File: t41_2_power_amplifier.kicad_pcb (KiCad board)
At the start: 2 copper layers, 100 x 100 mm, 72 parts, among them J1 5-1814832-1, J2 5-1814832-1, J3 B2B-XH-A_LF__SN_, J5 Screw_Terminal_01x02, Q1 Q_NMOS_GSD, Q2 Q_NPN_BCE, Q3 Q_NMOS_GSD, Q4 Q_NPN_BCE, Q5 Q_PMOS_GSD, Q6 Q_NPN_BEC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

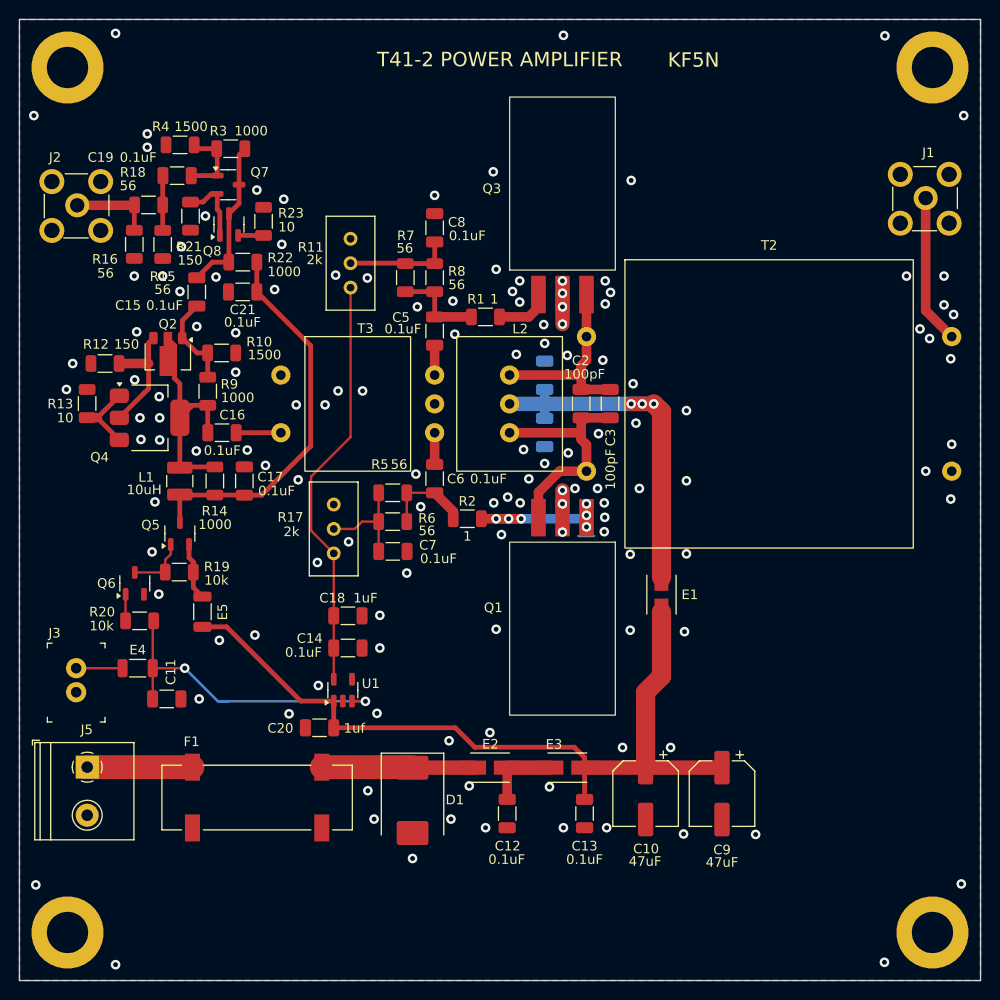
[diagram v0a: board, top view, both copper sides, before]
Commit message: Power Amplifier module ready for fab.
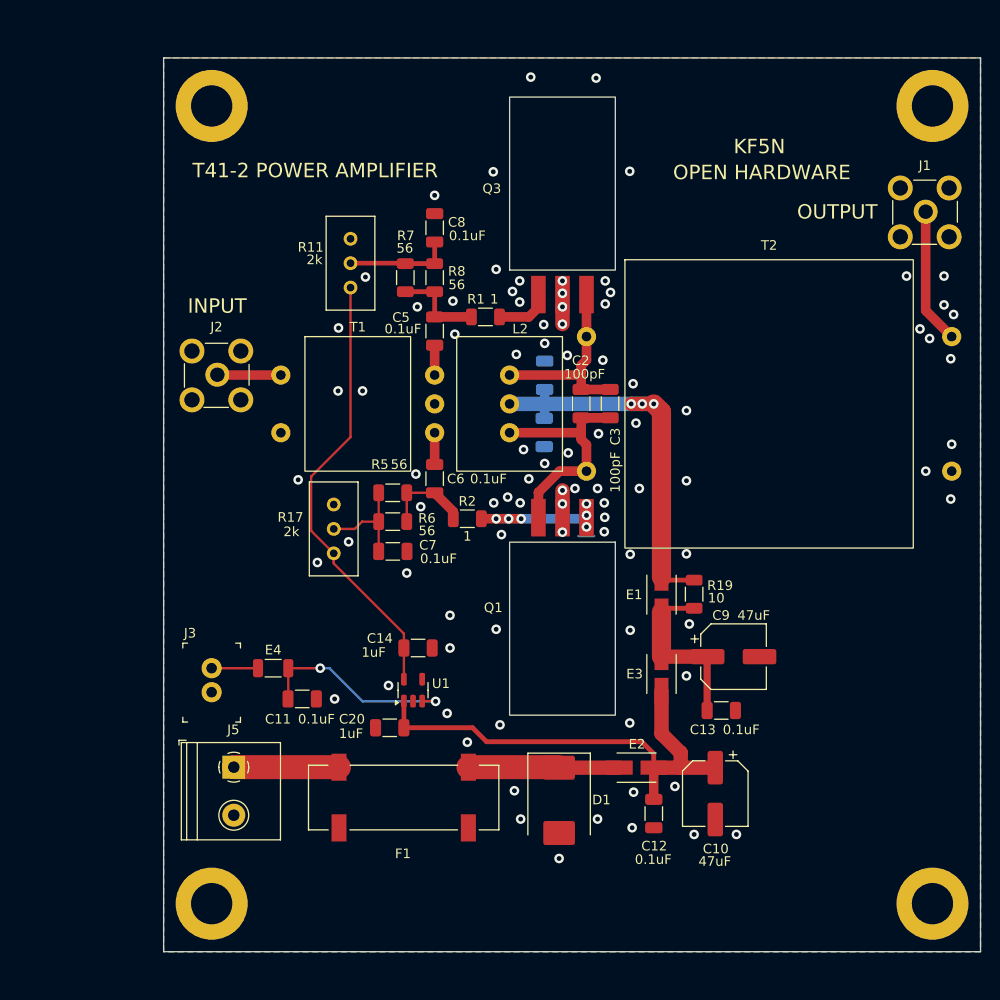
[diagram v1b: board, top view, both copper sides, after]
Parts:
- removed C15, C16, C17, C19, C21: 0.1uF, Capacitor_SMD:C_1206_3216Metric
- removed C18: 1uF, Capacitor_SMD:C_1206_3216Metric
- removed E5: XXX, Inductor_SMD:L_1206_3216Metric
- removed L1: 10uH, Inductor_SMD:L_1210_3225Metric
- removed Q2: Q_NPN_BCE, Package_TO_SOT_SMD:SOT-89-3
- removed Q4: Q_NPN_BCE, Package_TO_SOT_SMD:SOT-223
- removed Q5: Q_PMOS_GSD, Package_TO_SOT_SMD:SOT-23-3
- removed Q6, Q7, Q8: Q_NPN_BEC, Package_TO_SOT_SMD:SOT-23-3
- removed R10, R4: 1500, Resistor_SMD:R_1206_3216Metric
- removed R12, R21: 150, Resistor_SMD:R_1206_3216Metric
- removed R13, R23: 10, Resistor_SMD:R_1206_3216Metric
- removed R14, R22, R3, R9: 1000, Resistor_SMD:R_1206_3216Metric
- removed R15, R16, R18: 56, Resistor_SMD:R_1206_3216Metric
- removed R20: 10k, Resistor_SMD:R_1206_3216Metric
- removed T3: Transformer_1P_SS, Binocular_Core:BN-43-302
- added T1: Transformer_1P_SS, Binocular_Core:BN-43-302, F.Cu at (135.2, 90.0)
- C14: value 0.1uF -> 1uF
- C20: value 1uf -> 1uF
- R19: value 10k -> 10
- moved R19 53.6 mm to (170.2, 109.8), turned to 90 degrees
- moved J2 22.9 mm to (120.5, 87.0)
- moved C13 17.8 mm to (173.0, 121.9), turned to 0 degrees
- moved H1 15.5 mm to (120.0, 59.0)
- moved H2 15.3 mm to (120.0, 142.0)
- moved C12 15.2 mm to (166.0, 132.6)
- moved D1 15.2 mm to (156.2, 131.2)
- moved E2 15.2 mm to (164.2, 127.8)
- moved J5 15.2 mm to (122.3, 127.8)
- moved F1 15.2 mm to (140.0, 131.0)
- moved C9 14.3 mm to (174.3, 116.3), turned to 0 degrees
- moved E4 14.1 mm to (126.4, 117.5)
- moved J3 14.1 mm to (120.0, 117.5)
- moved C11 14.1 mm to (129.4, 120.7)
- moved E3 13.8 mm to (166.8, 118.1), turned to 90 degrees
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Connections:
- C1 pad 1: /12V_OUT_FIL -> /12V_PA
- C10 pad 1: Net-(U1-VIN) -> /12V_FIL
- C12 pad 1: Net-(C12-Pad1) -> /12V_FIL
- C13 pad 1: Net-(U1-VIN) -> Net-(C13-Pad1)
- C20 pad 1: Net-(U1-VIN) -> /12V_FIL
- C4 pad 1: /12V_OUT_FIL -> /12V_PA
- C9 pad 1: Net-(U1-VIN) -> Net-(C13-Pad1)
- E1 pad 1: Net-(U1-VIN) -> Net-(C13-Pad1)
- E1 pad 2: /12V_OUT_FIL -> /12V_PA
- E2 pad 2: Net-(C12-Pad1) -> /12V_FIL
- E3 pad 1: Net-(C12-Pad1) -> /12V_FIL
- E3 pad 2: Net-(U1-VIN) -> Net-(C13-Pad1)
- L2 pad 2: /12V_OUT_FIL -> /12V_PA
- R19 pad 1: Net-(Q5-G) -> Net-(C13-Pad1)
- R19 pad 2: Net-(Q5-S) -> /12V_PA
- U1 pad 1: Net-(U1-VIN) -> /12V_FIL
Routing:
- net Net-(U1-VIN): track 82.6 -> 0.00 mm
- net /12V_FIL: track 0.00 -> 49.9 mm
- net /12V_PA: track 0.00 -> 42.3 mm, vias 0 -> 3
- net /12V_IN_FIL: track 40.2 -> 0.00 mm
- net /12V_OUT_FIL: track 38.7 -> 0.00 mm, vias 3 -> 0
- net Net-(Q2-C): track 24.0 -> 0.00 mm
- net Net-(C13-Pad1): track 0.00 -> 18.7 mm
- net Net-(Q7-C): track 16.5 -> 0.00 mm
- net Net-(Q2-E): track 12.8 -> 0.00 mm
- net /TXRX: track 34.0 -> 21.4 mm
- net Net-(Q2-B): track 9.77 -> 0.00 mm
- net Net-(Q7-B): track 8.07 -> 0.00 mm
- net Net-(C12-Pad1): track 7.77 -> 0.00 mm
- net Net-(Q7-E): track 7.57 -> 0.00 mm
- net Net-(Q4-E): track 7.56 -> 0.00 mm
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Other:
- board size 100 x 100 mm -> 85 x 93 mm
- board text added: "INPUT"
- board text added: "OPEN HARDWARE"
- board text added: "OUTPUT"

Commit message: Larger output balun design to fab.
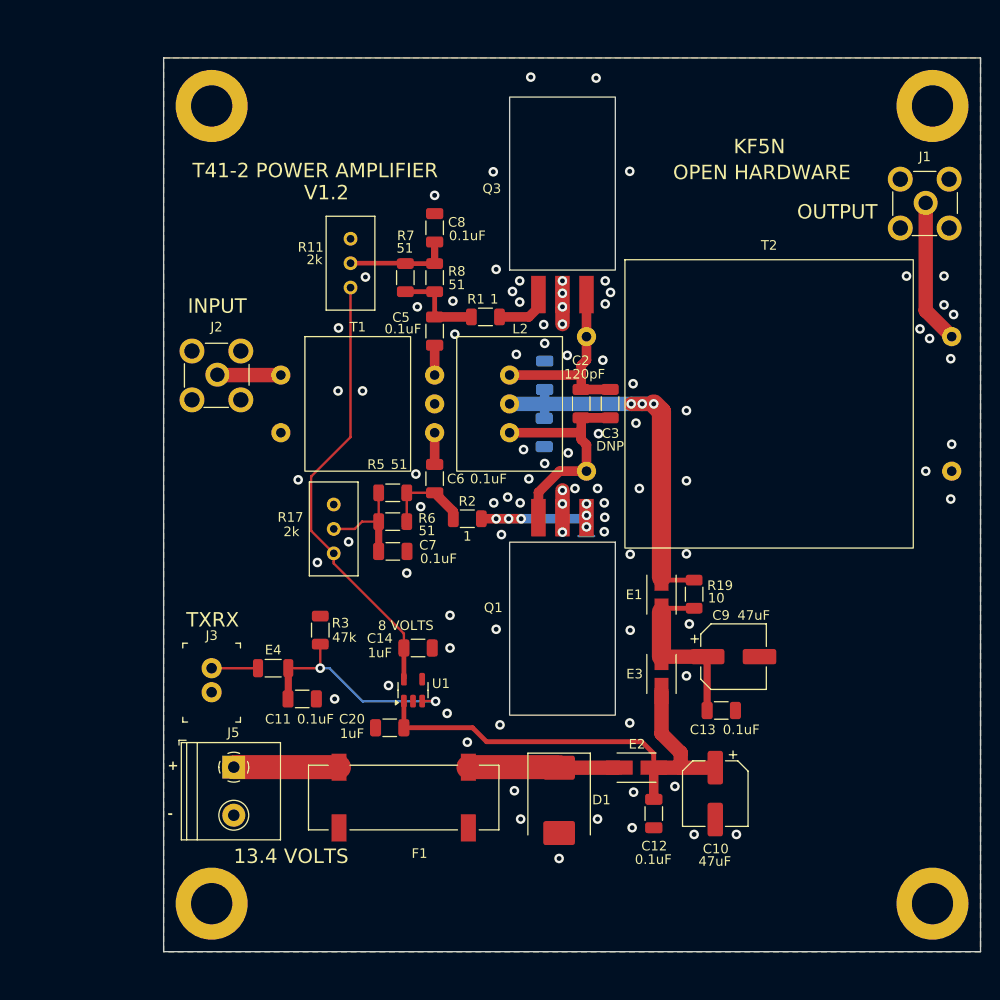
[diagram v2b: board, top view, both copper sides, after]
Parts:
- added R3: 47k, Resistor_SMD:R_1206_3216Metric, F.Cu at (131.3, 113.5)
- C2: value 100pF -> 120pF
- C3: value 100pF -> DNP
- E4: value XXX -> FerriteBead_Small
- R5, R6, R7, R8: value 56 -> 51
- moved J1 0.92 mm to (194.2, 69.2)
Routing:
- net /TXRX: track 21.4 -> 23.9 mm
- net Net-(T2-SB): track 14.1 -> 15.0 mm
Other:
- board text added: "+"
- board text added: "-"
- board text added: "13.4 VOLTS"
- board text added: "8 VOLTS"
- board text added: "TXRX"
- board text added: "V1.2"

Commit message: T41-2 Power Amplifier S to fab.
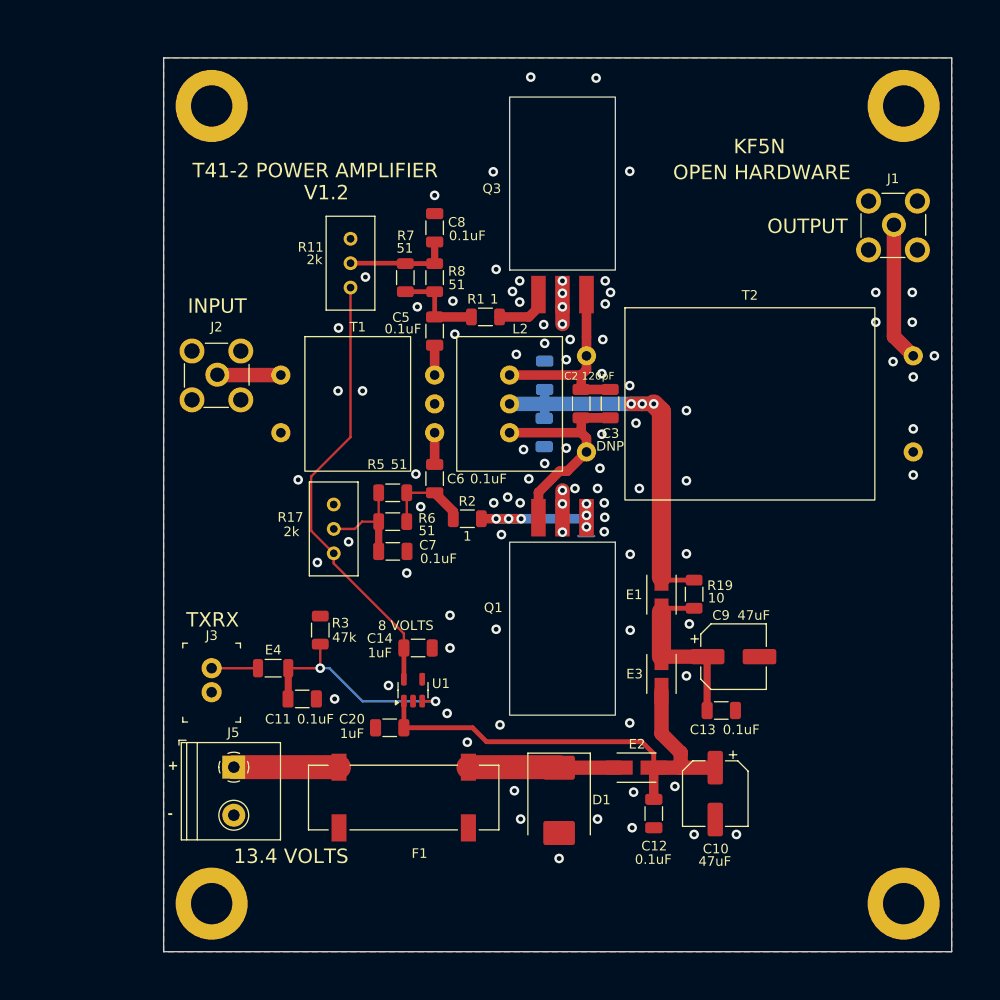
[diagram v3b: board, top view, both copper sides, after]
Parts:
- T2: footprint Binocular_Core:BN-43-7051 -> Binocular_Core:BN-43-3312
- moved J1 4.01 mm to (190.9, 71.4)
- moved H3 3.00 mm to (192.0, 142.0)
- moved H4 3.00 mm to (192.0, 59.0)
- moved T2 2.00 mm to (176.0, 90.0)
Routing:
- net Net-(Q1-D): track 25.4 -> 24.2 mm
- net Net-(T2-SB): track 15.0 -> 14.5 mm
- net GND: vias 89 -> 91
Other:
- board size 85 x 93 mm -> 82 x 93 mm

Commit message: Power Amplifier to fab.
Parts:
- moved J5 1.30 mm to (123.6, 127.8)
- moved J1 0.98 mm to (190.9, 70.5)
- moved J3 0.91 mm to (120.9, 117.5)
- moved C11 0.78 mm to (130.2, 120.7)
- moved E4 0.73 mm to (127.1, 117.5)
- moved F1 0.62 mm to (140.6, 131.0)
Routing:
- net Net-(T2-SB): track 14.5 -> 15.4 mm
- net /TXRX: track 23.9 -> 23.2 mm
- net Net-(J5-Pin_1): track 11.0 -> 10.3 mm
- net Net-(D1-K): track 15.7 -> 15.2 mm
- net GND: vias 91 -> 93
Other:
- board text added: "IN"
- board text added: "V1.3"
- board text removed: "V1.2"
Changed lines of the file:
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@@
 		(pad "4" thru_hole circle
 			(at 8 0)
-			(size 2 2)
-			(drill 1)
+			(size 2.2 2.2)
+			(drill 1.2)
 			(layers "*.Cu" "*.Mask")
 			(remove_unused_layers no)
@@
 	(footprint "3587TR:FUSE_3587TR"
 		(layer "F.Cu")
-		(at 139.98 130.96)
+		(at 140.6 130.96)
 		(property "Reference" "F1"
-			(at 1.645 5.815 0)
+			(at 0 5.84 0)
 			(layer "F.SilkS")
 			(effects
@@
 	(footprint "Capacitor_SMD:C_1206_3216Metric"
 		(layer "F.Cu")
-		(at 129.42 120.7 180)
+		(at 130.2 120.7 180)
 		(descr "Capacitor SMD 1206 (3216 Metric), square (rectangular) end terminal, IPC_7351 nominal, (Body size source: IPC-SM-782 page 76, https://www.pcb-3d.com/wordpress/wp-content/uploads/ipc-sm-782a_amendment_1_and_2.pdf), generated with kicad-footprint-generator")
 		(tags "capacitor")
 		(property "Reference" "C11"
-			(at 2.52 -2.1 180)
+			(at 3.3 -2.1 180)
 			(layer "F.SilkS")
 			(effects
@@
 		)
 		(property "Value" "0.1uF"
-			(at -1.38 -2.1 180)
+			(at -0.6 -2.1 180)
 			(layer "F.SilkS")
 			(effects
@@
 	(footprint "digikey-footprints:RF_SMA_Vertical_5-1814832-1"
 		(layer "F.Cu")
-		(at 190.89 71.44)
+		(at 190.89 70.46)
 		(property "Reference" "J1"
 			(at 0.01 -4.875 0)
@@
 	(footprint "TerminalBlock_Philmore:TerminalBlock_Philmore_TB132_1x02_P5.00mm_Horizontal"
 		(layer "F.Cu")
-		(at 122.3 127.8 -90)
+		(at 123.6 127.8 -90)
 		(descr "Terminal Block Philmore , 2 pins, pitch 5mm, size 10x10.2mm^2, drill diamater 1.2mm, pad diameter 2.4mm, see http://www.philmore-datak.com/mc/Page%20197.pdf, script-generated using https://github.com/pointhi/kicad-footprint-generator/scripts/TerminalBlock_Philmore")
 		(tags "THT Terminal Block Philmore  pitch 5mm size 10x10.2mm^2 drill 1.2mm pad 2.4mm")
 		(property "Reference" "J5"
-			(at -3.6 0.05 180)
+			(at -3.6 0.05 360)
 			(layer "F.SilkS")
 			(effects
@@
 	(footprint "digikey-footprints:PinHeader_1x2_P2.5mm_Drill1.1mm"
 		(layer "F.Cu")
-		(at 119.995 117.5 -90)
+		(at 120.9 117.5 -90)
 		(descr "http://www.jst-mfg.com/product/pdf/eng/eXH.pdf")
 		(property "Reference" "J3"
-			(at -3.4 -0.005 180)
+			(at -3.4 -0.005 360)
 			(layer "F.SilkS")
 			(effects
@@
 	(footprint "Inductor_SMD:L_1206_3216Metric"
 		(layer "F.Cu")
-		(at 126.395 117.5)
+		(at 127.125 117.5)
 		(descr "Inductor SMD 1206 (3216 Metric), square (rectangular) end terminal, IPC_7351 nominal, (Body size source: IPC-SM-782 page 80, https://www.pcb-3d.com/wordpress/wp-content/uploads/ipc-sm-782a_amendment_1_and_2.pdf), generated with kicad-footprint-generator")
 		(tags "inductor")
@@
 		(pad "2" thru_hole circle
 			(at 0 0)
-			(size 2 2)
-			(drill 1)
+			(size 2.2 2.2)
+			(drill 1.2)
 			(layers "*.Cu" "*.Mask")
 			(remove_unused_layers no)
@@
 	)
 	(gr_text "+"
-		(at 115.4 128.2 0)
+		(at 115.2 128.7 0)
 		(layer "F.SilkS")
 		(effects
 			(font
-				(size 1 1)
-				(thickness 0.2)
-				(bold yes)
+				(size 2 2)
+				(thickness 0.3)
 			)
 			(justify left bottom)
@@
 	)
 	(gr_text "-"
-		(at 115.4 133.2 0)
+		(at 115.2 133.7 0)
 		(layer "F.SilkS")
 		(effects
 			(font
-				(size 1 1)
-				(thickness 0.2)
-				(bold yes)
+				(size 2 2)
+				(thickness 0.3)
 			)
 			(justify left bottom)
@@
 		)
 	)
-	(gr_text "V1.2"
+	(gr_text "IN"
+		(at 115.4 118.4 0)
+		(layer "F.SilkS")
+		(effects
+			(font
+				(size 1.5 1.5)
+				(thickness 0.2)
+			)
+			(justify left bottom)
+		)
+	)
+	(gr_text "V1.3"
 		(at 129.6 68.9 0)
 		(layer "F.SilkS")
@@
 	)
 	(gr_text "TXRX"
-		(at 117.35 113.35 0)
+		(at 118.1 113.2 0)
 		(layer "F.SilkS")
 		(effects
@@
 	)
 	(via
+		(at 133.1 116.3)
+		(size 1)
+		(drill 0.5)
+		(layers "F.Cu" "B.Cu")
+		(free yes)
+		(net 2)
+	)
+	(via
 		(at 150.15 103.6)
 		(size 1)
@@
 	)
 	(via
+		(at 180.4 116.3)
+		(size 1)
+		(drill 0.5)
+		(layers "F.Cu" "B.Cu")
+		(free yes)
+		(net 2)
+	)
+	(via
 		(at 174.6 134.8)
 		(size 1)
@@
 	)
 	(via
-		(at 132.795 120.7)
+		(at 133.6 120.7)
 		(size 1)
 		(drill 0.5)
@@
 	(segment
 		(start 131.295 117.5)
-		(end 131.3 117.495)
+		(end 128.7 117.5)
 		(width 0.25)
 		(layer "F.Cu")
@@
 	)
 	(segment
-		(start 131.3 117.495)
-		(end 131.3 115)
+		(start 128.7 120.675)
+		(end 128.725 120.7)
 		(width 0.25)
 		(layer "F.Cu")
@@
 	)
 	(segment
-		(start 143.275 120.925)
-		(end 143.3 120.95)
+		(start 131.295 117.5)
+		(end 131.3 117.495)
 		(width 0.25)
 		(layer "F.Cu")
@@
 	)
 	(segment
-		(start 127.97 120.675)
-		(end 127.945 120.7)
+		(start 131.3 117.495)
+		(end 131.3 115)
 		(width 0.25)
 		(layer "F.Cu")
@@
 	)
 	(segment
-		(start 131.295 117.5)
-		(end 127.97 117.5)
-		(width 0.25)
+		(start 128.7 117.5)
+		(end 128.7 120.675)
+		(width 0.75)
 		(layer "F.Cu")
 		(net 12)
 	)
 	(segment
-		(start 141.9 120.925)
-		(end 143.275 120.925)
+		(start 143.275 120.925)
+		(end 143.3 120.95)
 		(width 0.25)
 		(layer "F.Cu")
@@
 	)
 	(segment
-		(start 127.97 117.5)
-		(end 127.97 120.675)
-		(width 0.75)
+		(start 141.9 120.925)
+		(end 143.275 120.925)
+		(width 0.25)
 		(layer "F.Cu")
 		(net 12)
@@
 	)
 	(segment
-		(start 146.71 127.8)
-		(end 156.1 127.8)
+		(start 156.15 127.85)
+		(end 147.38 127.85)
 		(width 2.5)
 		(layer "F.Cu")
@@
 	)
 	(segment
+		(start 147.38 127.85)
+		(end 147.33 127.8)
+		(width 1)
+		(layer "F.Cu")
+		(net 15)
+	)
+	(segment
 		(start 156.15 127.85)
 		(end 162.42 127.85)
@@
 	)
 	(segment
-		(start 119.995 117.5)
-		(end 124.82 117.5)
+		(start 120.9 117.5)
+		(end 125.55 117.5)
 		(width 0.25)
 		(layer "F.Cu")
@@
 	)
 	(segment
-		(start 122.3 127.8)
-		(end 133.25 127.8)
+		(start 133.87 127.8)
+		(end 123.6 127.8)
 		(width 2.5)
 		(layer "F.Cu")
@@
 	(segment
 		(start 191 83)
-		(end 193 85)
+		(end 191 80)
+		(width 1.5)
+		(layer "F.Cu")
+		(net 18)
+	)
+	(segment
+		(start 190.99 79.99)
+		(end 190.99 70.385)
 		(width 1.5)
 		(layer "F.Cu")
@@
 	)
 	(segment
-		(start 190.99 83)
-		(end 191 83)
+		(start 191 83)
+		(end 193 85)
 		(width 1.5)
 		(layer "F.Cu")
@@
 	)
 	(segment
-		(start 190.99 71.365)
-		(end 190.99 83)
+		(start 191 80)
+		(end 190.99 79.99)
 		(width 1.5)
 		(layer "F.Cu")
@@
 		(polygon
 			(pts
-				(xy 128.685 121.6) (xy 128.685 119.78) (xy 130.107504 119.78) (xy 130.107504 121.6)
+				(xy 129.485 121.6) (xy 129.485 119.78) (xy 130.907504 119.78) (xy 130.907504 121.6)
 			)
 		)

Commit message: Released to fab.
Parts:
- removed C2: 120pF, Capacitor_SMD:C_1206_3216Metric
- removed C3: DNP, Capacitor_SMD:C_1206_3216Metric
- added C15: 0.1uF, Capacitor_SMD:C_1206_3216Metric, B.Cu at (166.9, 85.6)
- added C16: 0.1uF, Capacitor_SMD:C_1206_3216Metric, B.Cu at (166.9, 94.4)
- added T3: Transformer_1P_1S, Binocular_Core:BN-43-202, F.Cu at (172.7, 97.4)
- T2: footprint Binocular_Core:BN-43-3312 -> Binocular_Core:BN-43-202
- moved T2 8.10 mm to (172.7, 82.6)
- moved H3 4.00 mm to (188.0, 142.0)
- moved H4 4.00 mm to (188.0, 59.0)
- moved J1 3.92 mm to (187.0, 70.0)
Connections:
- T2 pad 2: Net-(Q1-D) -> /12V_PA
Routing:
- net Net-(T2-SB): track 15.4 -> 37.7 mm
- net /12V_PA: track 42.3 -> 57.3 mm
- net Net-(Q3-D): track 21.1 -> 23.3 mm
- net Net-(Q1-D): track 24.2 -> 26.1 mm
- net GND: vias 93 -> 105
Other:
- board size 82 x 93 mm -> 78 x 93 mm
- board text added: "V1.4"
- board text removed: "V1.3"
